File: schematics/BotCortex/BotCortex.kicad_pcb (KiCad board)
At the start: 2 copper layers, 61 parts, among them P1 2x Serial, P10 Stepper Upperarm, P11 Stepper Hip, P12 POWER_IN, P13 PowerEnableIn, P14 Power Stepper 2, P15 Power Stepper 3, P16 Power Stepper 4, P17 PowerEnableOut, P18 Power Stepper 5, P19 ODroid Power, P2 Herkulex Servo, P20 POTI 10K, P21 Reset_Conn, P22 Reset Conn, P23 LED-Driver-I2C, P24 UART6, P25 Thermal_Printer, P26 Reset Anschluss, P28 Power Stepper 1, P3 Encoder Socket 1, P4 Encoder Socket 0, P5 Stepper Elbow, P6 Power In uC Servo 9V, P7 Power Out uC Servo, P8 Stepper Forearm, P9 Stepper Wrist, Q1 BC237, Q2 BC237, SW2 reset, U1 7805, U2 LM7809ACT, U3 LM7809ACT, U4 Teensy_3.5

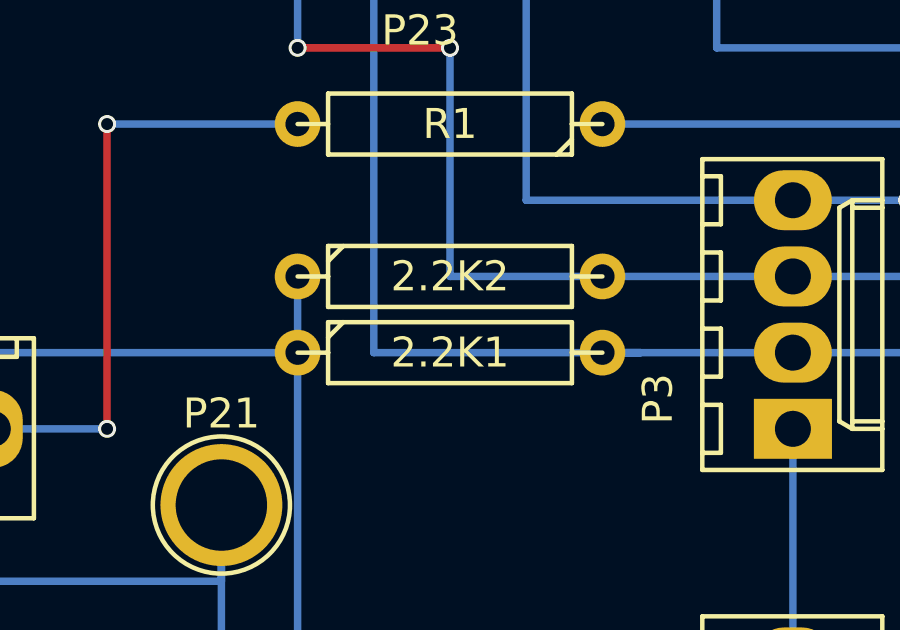
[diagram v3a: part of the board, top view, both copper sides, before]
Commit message: reduced pullup resistors in I2C lines
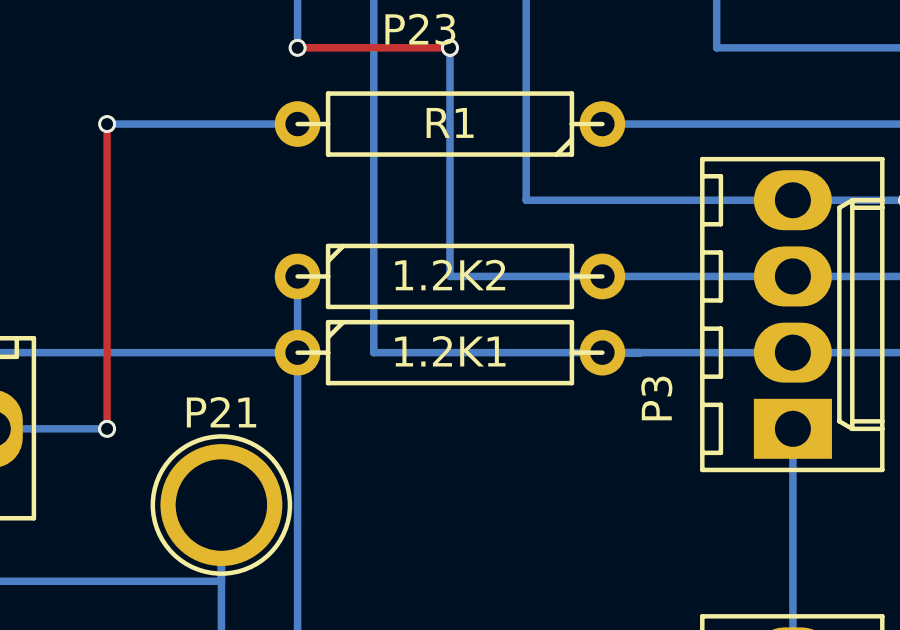
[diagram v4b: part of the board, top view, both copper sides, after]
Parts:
- removed 2.2K1, 2.2K2: R, Discret:R4
- added 1.2K1: R, Discret:R4, F.Cu at (146.1, 63.5)
- added 1.2K2: R, Discret:R4, F.Cu at (146.1, 61.0)
- P19: value ODroid Power -> Thermal Printer 5V
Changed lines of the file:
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@@
       (effects (font (size 1 1) (thickness 0.15)))
     )
-    (fp_text value "ODroid Power" (at 0 5.08 270) (layer F.Fab)
+    (fp_text value "Thermal Printer 5V" (at 0 5.08 270) (layer F.Fab)
       (effects (font (size 1 1) (thickness 0.15)))
     )
@@
   )
   (module Discret:R4 (layer F.Cu)
-    (at 146.05 63.5)
-    (descr "Resitance 4 pas")
-    (tags R)
-    (fp_text reference 2.2K1 (at 0 0) (layer F.SilkS)
-      (effects (font (size 1 1) (thickness 0.15)))
-    )
-    (fp_text value R (at 0 0) (layer F.Fab)
-      (effects (font (size 1 1) (thickness 0.15)))
-    )
-    (fp_line (start -5.08 0) (end -4.064 0) (layer F.SilkS) (width 0.15))
-    (fp_line (start -4.064 0) (end -4.064 -1.016) (layer F.SilkS) (width 0.15))
-    (fp_line (start -4.064 -1.016) (end 4.064 -1.016) (layer F.SilkS) (width 0.15))
-    (fp_line (start 4.064 -1.016) (end 4.064 1.016) (layer F.SilkS) (width 0.15))
-    (fp_line (start 4.064 1.016) (end -4.064 1.016) (layer F.SilkS) (width 0.15))
-    (fp_line (start -4.064 1.016) (end -4.064 0) (layer F.SilkS) (width 0.15))
-    (fp_line (start -4.064 -0.508) (end -3.556 -1.016) (layer F.SilkS) (width 0.15))
-    (fp_line (start 5.08 0) (end 4.064 0) (layer F.SilkS) (width 0.15))
-    (pad 1 thru_hole circle (at -5.08 0) (size 1.524 1.524) (drill 0.8128) (layers *.Cu *.Mask F.SilkS)
-      (net 46 /3.3V))
-    (pad 2 thru_hole circle (at 5.08 0) (size 1.524 1.524) (drill 0.8128) (layers *.Cu *.Mask F.SilkS)
-      (net 36 /SDA1))
-    (model Discret.3dshapes/R4.wrl
-      (at (xyz 0 0 0))
-      (scale (xyz 0.4 0.4 0.4))
-      (rotate (xyz 0 0 0))
-    )
-  )
-  (module Discret:R4 (layer F.Cu)
-    (at 146.05 60.96)
-    (descr "Resitance 4 pas")
-    (tags R)
-    (fp_text reference 2.2K2 (at 0 0) (layer F.SilkS)
-      (effects (font (size 1 1) (thickness 0.15)))
-    )
-    (fp_text value R (at 0 0) (layer F.Fab)
-      (effects (font (size 1 1) (thickness 0.15)))
-    )
-    (fp_line (start -5.08 0) (end -4.064 0) (layer F.SilkS) (width 0.15))
-    (fp_line (start -4.064 0) (end -4.064 -1.016) (layer F.SilkS) (width 0.15))
-    (fp_line (start -4.064 -1.016) (end 4.064 -1.016) (layer F.SilkS) (width 0.15))
-    (fp_line (start 4.064 -1.016) (end 4.064 1.016) (layer F.SilkS) (width 0.15))
-    (fp_line (start 4.064 1.016) (end -4.064 1.016) (layer F.SilkS) (width 0.15))
-    (fp_line (start -4.064 1.016) (end -4.064 0) (layer F.SilkS) (width 0.15))
-    (fp_line (start -4.064 -0.508) (end -3.556 -1.016) (layer F.SilkS) (width 0.15))
-    (fp_line (start 5.08 0) (end 4.064 0) (layer F.SilkS) (width 0.15))
-    (pad 1 thru_hole circle (at -5.08 0) (size 1.524 1.524) (drill 0.8128) (layers *.Cu *.Mask F.SilkS)
-      (net 46 /3.3V))
-    (pad 2 thru_hole circle (at 5.08 0) (size 1.524 1.524) (drill 0.8128) (layers *.Cu *.Mask F.SilkS)
-      (net 37 /SCl1))
-    (model Discret.3dshapes/R4.wrl
-      (at (xyz 0 0 0))
-      (scale (xyz 0.4 0.4 0.4))
-      (rotate (xyz 0 0 0))
-    )
-  )
-  (module Discret:R4 (layer F.Cu)
     (at 147.32 86.36 270)
     (descr "Resitance 4 pas")
@@
     )
   )
+  (module Discret:R4 (layer F.Cu)
+    (at 146.05 63.5)
+    (descr "Resitance 4 pas")
+    (tags R)
+    (fp_text reference 1.2K1 (at 0 0) (layer F.SilkS)
+      (effects (font (size 1 1) (thickness 0.15)))
+    )
+    (fp_text value R (at 0 0) (layer F.Fab)
+      (effects (font (size 1 1) (thickness 0.15)))
+    )
+    (fp_line (start -5.08 0) (end -4.064 0) (layer F.SilkS) (width 0.15))
+    (fp_line (start -4.064 0) (end -4.064 -1.016) (layer F.SilkS) (width 0.15))
+    (fp_line (start -4.064 -1.016) (end 4.064 -1.016) (layer F.SilkS) (width 0.15))
+    (fp_line (start 4.064 -1.016) (end 4.064 1.016) (layer F.SilkS) (width 0.15))
+    (fp_line (start 4.064 1.016) (end -4.064 1.016) (layer F.SilkS) (width 0.15))
+    (fp_line (start -4.064 1.016) (end -4.064 0) (layer F.SilkS) (width 0.15))
+    (fp_line (start -4.064 -0.508) (end -3.556 -1.016) (layer F.SilkS) (width 0.15))
+    (fp_line (start 5.08 0) (end 4.064 0) (layer F.SilkS) (width 0.15))
+    (pad 1 thru_hole circle (at -5.08 0) (size 1.524 1.524) (drill 0.8128) (layers *.Cu *.Mask F.SilkS)
+      (net 46 /3.3V))
+    (pad 2 thru_hole circle (at 5.08 0) (size 1.524 1.524) (drill 0.8128) (layers *.Cu *.Mask F.SilkS)
+      (net 36 /SDA1))
+    (model Discret.3dshapes/R4.wrl
+      (at (xyz 0 0 0))
+      (scale (xyz 0.4 0.4 0.4))
+      (rotate (xyz 0 0 0))
+    )
+  )
+  (module Discret:R4 (layer F.Cu)
+    (at 146.05 60.96)
+    (descr "Resitance 4 pas")
+    (tags R)
+    (fp_text reference 1.2K2 (at 0 0) (layer F.SilkS)
+      (effects (font (size 1 1) (thickness 0.15)))
+    )
+    (fp_text value R (at 0 0) (layer F.Fab)
+      (effects (font (size 1 1) (thickness 0.15)))
+    )
+    (fp_line (start -5.08 0) (end -4.064 0) (layer F.SilkS) (width 0.15))
+    (fp_line (start -4.064 0) (end -4.064 -1.016) (layer F.SilkS) (width 0.15))
+    (fp_line (start -4.064 -1.016) (end 4.064 -1.016) (layer F.SilkS) (width 0.15))
+    (fp_line (start 4.064 -1.016) (end 4.064 1.016) (layer F.SilkS) (width 0.15))
+    (fp_line (start 4.064 1.016) (end -4.064 1.016) (layer F.SilkS) (width 0.15))
+    (fp_line (start -4.064 1.016) (end -4.064 0) (layer F.SilkS) (width 0.15))
+    (fp_line (start -4.064 -0.508) (end -3.556 -1.016) (layer F.SilkS) (width 0.15))
+    (fp_line (start 5.08 0) (end 4.064 0) (layer F.SilkS) (width 0.15))
+    (pad 1 thru_hole circle (at -5.08 0) (size 1.524 1.524) (drill 0.8128) (layers *.Cu *.Mask F.SilkS)
+      (net 46 /3.3V))
+    (pad 2 thru_hole circle (at 5.08 0) (size 1.524 1.524) (drill 0.8128) (layers *.Cu *.Mask F.SilkS)
+      (net 37 /SCl1))
+    (model Discret.3dshapes/R4.wrl
+      (at (xyz 0 0 0))
+      (scale (xyz 0.4 0.4 0.4))
+      (rotate (xyz 0 0 0))
+    )
+  )
   (target plus (at 91.44 33.02) (size 5) (width 0.1) (layer Edge.Cuts))
   (target plus (at 109.22 125.73) (size 5) (width 0.1) (layer Edge.Cuts))
@@
   (segment (start 182.88 76.2) (end 196.85 76.2) (width 0.25) (layer B.Cu) (net 1) (status 10))
   (segment (start 198.12 73.66) (end 198.12 73.66) (width 0.25) (layer B.Cu) (net 1) (status 30))
-  (segment (start 118.11 66.04) (end 125.73 66.04) (width 0.25) (layer B.Cu) (net 2) (status 800000))
+  (segment (start 118.11 66.04) (end 125.73 66.04) (width 0.25) (layer B.Cu) (net 2))
   (segment (start 138.43 48.26) (end 138.43 45.72) (width 0.25) (layer B.Cu) (net 2))
   (segment (start 114.3 111.76) (end 114.3 114.3) (width 0.25) (layer B.Cu) (net 2))
@@
   (segment (start 125.73 78.74) (end 125.73 78.74) (width 0.25) (layer B.Cu) (net 53) (status 30))
   (segment (start 140.97 55.88) (end 134.62 55.88) (width 0.25) (layer B.Cu) (net 54))
-  (segment (start 134.62 66.04) (end 130.81 66.04) (width 0.25) (layer B.Cu) (net 54) (status 800020))
+  (segment (start 134.62 66.04) (end 130.81 66.04) (width 0.25) (layer B.Cu) (net 54) (status 20))
   (via (at 134.62 66.04) (size 0.6) (drill 0.4) (layers F.Cu B.Cu) (net 54))
   (segment (start 134.62 55.88) (end 134.62 66.04) (width 0.25) (layer F.Cu) (net 54))
